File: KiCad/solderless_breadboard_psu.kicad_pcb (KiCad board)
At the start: 4 copper layers, 55 x 51 mm, 87 parts, among them IC301 MCP73831T-2ACI_OT, IC302 BQ29737DSER, IC401 TLV62569DBVR, IC501 FT232RL-REEL, J201 Barrel_Jack_Switch_Pin3Ring, J301 BM02B-GHS-TBT_LF__SN__N_, J501 Conn_01x09_Pin, J502 Conn_01x09_Pin, J503 Conn_01x06_Pin, J504 USB_C_Receptacle_USB2.0_16P, J601 Conn_02x03_Odd_Even, J602 Conn_02x03_Odd_Even, Q301 DMG3415U-7, Q302 T2N7002AK, Q303 T2N7002AK, U401 TPS61040DBVR, U501 USBLC6-2SC6

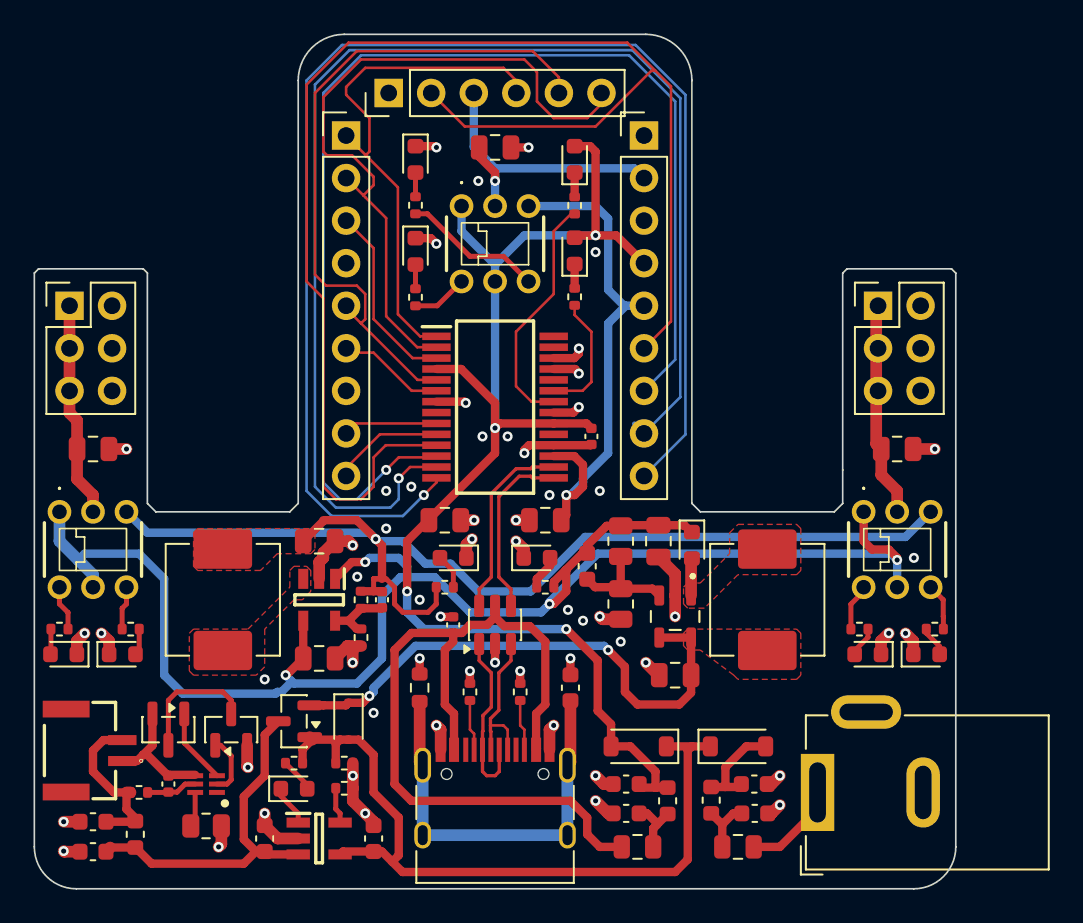
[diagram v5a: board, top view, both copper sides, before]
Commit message: PCB DRC fixes
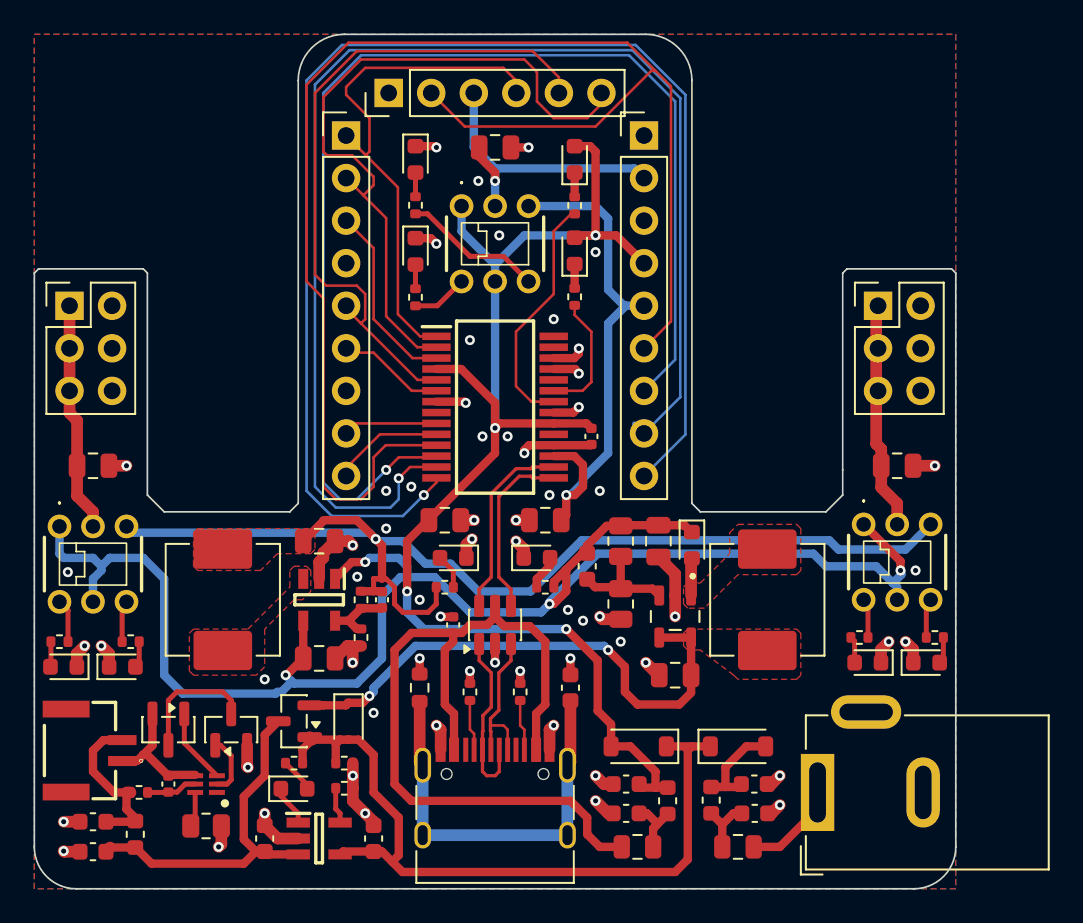
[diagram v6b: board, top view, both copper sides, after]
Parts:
- moved C601 1.00 mm to (26.0, 72.2)
- moved C602 1.00 mm to (74.0, 72.2)
- moved S601 0.87 mm to (24.0, 75.9)
- moved D601 0.75 mm to (24.2, 84.2)
- moved D602 0.75 mm to (27.8, 84.2)
- moved R601 0.75 mm to (24.0, 82.8)
- moved R602 0.75 mm to (28.2, 82.8)
- moved S602 0.75 mm to (72.0, 75.8)
- moved D603 0.50 mm to (72.2, 84.0)
- moved D604 0.50 mm to (75.8, 84.0)
- moved R603 0.50 mm to (71.8, 82.5), turned to 0 degrees
- moved R604 0.50 mm to (76.2, 82.5), turned to 180 degrees
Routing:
- net VCC_L: track 12.9 -> 13.8 mm
- net VCC_R: track 12.9 -> 13.6 mm
- net GND: vias 59 -> 63
- added copper zone on B.Cu, net GND
- added copper zone on F.Cu, net GND
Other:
- outline, holes or cut-outs redrawn

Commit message: Fill BOM table
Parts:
- C401, C402, C404, C406, C501, C503, C601, C602, C603: footprint Capacitor_SMD:C_0805_2012Metric -> Capacitor_SMD:C_0603_1608Metric
- R305, R402, R404: footprint Resistor_SMD:R_0805_2012Metric -> Resistor_SMD:R_0402_1005Metric
- R505: footprint Resistor_SMD:R_0603_1608Metric -> Resistor_SMD:R_0402_1005Metric
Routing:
- net GND: track 65.1 -> 65.8 mm, vias 63 -> 148
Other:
- board text added: "3V3"
- board text added: "5V"
- board text added: "CTS"
- board text added: "DCD"
- board text added: "DSR"
- board text added: "DTR"
- board text added: "FT232RL REEL"
- board text added: "GND"
- board text added: "PWREN"
- board text added: "RI"
- board text added: "RTS"
- board text added: "RX"
- board text added: "RXD"
- board text added: "SLP"
- board text added: "TEN"
- board text added: "TX"
- board text added: "TXD"
- board text added: "VCC"

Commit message: Production files
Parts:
- D401: footprint Diode_SMD:D_0603_1608Metric -> Diode_SMD:D_SMA
- R505: value DNP, 1MR -> 1MR
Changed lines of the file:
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@@
 			)
 		)
-		(property "Value" "DNP, 1MR"
+		(property "Value" "1MR"
 			(at 0 1.17 90)
 			(layer "F.Fab")
@@
 			(at 0 -1.17 0)
 			(layer "F.SilkS")
+			(hide yes)
 			(effects
 				(font
@@
 			(at 0 1.17 0)
 			(layer "F.Fab")
+			(hide yes)
 			(effects
 				(font
@@
 		)
 	)
-	(footprint "Diode_SMD:D_0603_1608Metric"
+	(footprint "Diode_SMD:D_SMA"
 		(layer "F.Cu")
 		(at 61.75 77 -90)
-		(descr "Diode SMD 0603 (1608 Metric), square (rectangular) end terminal, IPC-7351 nominal, (Body size source: http://www.tortai-tech.com/upload/download/2011102023233369053.pdf), generated with kicad-footprint-generator")
-		(tags "diode")
+		(descr "Diode SMA (DO-214AC)")
+		(tags "Diode SMA (DO-214AC)")
 		(property "Reference" "D401"
-			(at 0 -1.43 90)
+			(at 0 -2.5 270)
 			(layer "F.SilkS")
-			(hide yes)
 			(effects
 				(font
@@
 		)
 		(property "Value" "SS14"
-			(at 0 1.43 90)
+			(at 0 2.6 270)
 			(layer "F.Fab")
-			(hide yes)
 			(effects
 				(font
@@
 			)
 		)
-		(property "Datasheet" "https://www.vishay.com/docs/88746/ss12.pdf"
-			(at 0 0 90)
-			(layer "F.Fab")
-			(hide yes)
-			(effects
-				(font
-					(size 1.27 1.27)
-					(thickness 0.15)
-				)
-			)
-		)
-		(property "Description" "40V 1A Schottky Diode, SMA"
-			(at 0 0 90)
+		(property "Datasheet" "https://www.lcsc.com/datasheet/C266551.pdf"
+			(at 0 0 270)
+			(unlocked yes)
 			(layer "F.Fab")
 			(hide yes)
@@
 			)
 		)
-		(property "Manufacturer" "Schottky Diode"
+		(property "Description" "Diode 40V 1A Surface Mount SMA(DO-214AC)"
 			(at 0 0 270)
 			(unlocked yes)
@@
 			(effects
 				(font
-					(size 1 1)
+					(size 1.27 1.27)
 					(thickness 0.15)
 				)
 			)
 		)
-		(property "Manufacturer Product Number" "SD0603S040S0R2"
+		(property "Manufacturer" "BORN"
 			(at 0 0 270)
 			(unlocked yes)
@@
 			)
 		)
-		(property "Manufacturer Part Number" "JSMSEMI"
+		(property "Manufacturer Part Number" "SS14"
 			(at 0 0 270)
 			(unlocked yes)
@@
 		(attr smd)
 		(fp_line
-			(start -1.485 0.735)
-			(end 0.8 0.735)
+			(start -3.51 1.65)
+			(end 2 1.65)
 			(stroke
 				(width 0.12)
@@
 		)
 		(fp_line
-			(start -1.485 -0.735)
-			(end -1.485 0.735)
+			(start -3.51 -1.65)
+			(end -3.51 1.65)
 			(stroke
 				(width 0.12)
@@
 		)
 		(fp_line
-			(start 0.8 -0.735)
-			(end -1.485 -0.735)
+			(start -3.51 -1.65)
+			(end 2 -1.65)
 			(stroke
 				(width 0.12)
@@
 			(layer "F.SilkS")
 		)
-		(fp_rect
-			(start -1.48 -0.73)
-			(end 1.48 0.73)
+		(fp_line
+			(start -3.5 1.75)
+			(end -3.5 -1.75)
 			(stroke
 				(width 0.05)
 				(type solid)
 			)
-			(fill no)
 			(layer "F.CrtYd")
 		)
 		(fp_line
-			(start -0.8 0.4)
-			(end 0.8 0.4)
+			(start 3.5 1.75)
+			(end -3.5 1.75)
+			(stroke
+				(width 0.05)
+				(type solid)
+			)
+			(layer "F.CrtYd")
+		)
+		(fp_line
+			(start -3.5 -1.75)
+			(end 3.5 -1.75)
+			(stroke
+				(width 0.05)
+				(type solid)
+			)
+			(layer "F.CrtYd")
+		)
+		(fp_line
+			(start 3.5 -1.75)
+			(end 3.5 1.75)
+			(stroke
+				(width 0.05)
+				(type solid)
+			)
+			(layer "F.CrtYd")
+		)
+		(fp_line
+			(start -2.3 1.5)
+			(end -2.3 -1.5)
 			(stroke
 				(width 0.1)
@@
 		)
 		(fp_line
-			(start 0.8 0.4)
-			(end 0.8 -0.4)
+			(start 2.3 1.5)
+			(end -2.3 1.5)
 			(stroke
 				(width 0.1)
@@
 		)
 		(fp_line
-			(start -0.8 -0.1)
-			(end -0.8 0.4)
+			(start 0.50118 0.75032)
+			(end 0.50118 -0.79908)
 			(stroke
 				(width 0.1)
@@
 		)
 		(fp_line
-			(start -0.5 -0.4)
-			(end -0.8 -0.1)
+			(start -0.64944 0.00102)
+			(end 0.50118 0.75032)
 			(stroke
 				(width 0.1)
@@
 		)
 		(fp_line
-			(start 0.8 -0.4)
-			(end -0.5 -0.4)
+			(start -0.64944 0.00102)
+			(end -1.55114 0.00102)
+			(stroke
+				(width 0.1)
+				(type solid)
+			)
+			(layer "F.Fab")
+		)
+		(fp_line
+			(start -0.64944 0.00102)
+			(end 0.50118 -0.79908)
+			(stroke
+				(width 0.1)
+				(type solid)
+			)
+			(layer "F.Fab")
+		)
+		(fp_line
+			(start 0.50118 0.00102)
+			(end 1.4994 0.00102)
+			(stroke
+				(width 0.1)
+				(type solid)
+			)
+			(layer "F.Fab")
+		)
+		(fp_line
+			(start -0.64944 -0.79908)
+			(end -0.64944 0.80112)
+			(stroke
+				(width 0.1)
+				(type solid)
+			)
+			(layer "F.Fab")
+		)
+		(fp_line
+			(start 2.3 -1.5)
+			(end 2.3 1.5)
+			(stroke
+				(width 0.1)
+				(type solid)
+			)
+			(layer "F.Fab")
+		)
+		(fp_line
+			(start 2.3 -1.5)
+			(end -2.3 -1.5)
 			(stroke
 				(width 0.1)
@@
 		)
 		(fp_text user "${REFERENCE}"
-			(at 0 0 90)
+			(at 0 -2.5 270)
 			(layer "F.Fab")
 			(effects
 				(font
-					(size 0.4 0.4)
-					(thickness 0.06)
+					(size 1 1)
+					(thickness 0.15)
 				)
 			)
 		)
 		(pad "1" smd roundrect
-			(at -0.7875 0 270)
-			(size 0.875 0.95)
+			(at -2 0 270)
+			(size 2.5 1.8)
 			(layers "F.Cu" "F.Mask" "F.Paste")
-			(roundrect_rratio 0.25)
+			(roundrect_rratio 0.1388888889)
 			(net 11 "+5V")
 			(pinfunction "K")
@@
 		)
 		(pad "2" smd roundrect
-			(at 0.7875 0 270)
-			(size 0.875 0.95)
+			(at 2 0 270)
+			(size 2.5 1.8)
 			(layers "F.Cu" "F.Mask" "F.Paste")
-			(roundrect_rratio 0.25)
+			(roundrect_rratio 0.1388888889)
 			(net 21 "/[4]Buck Boost converter/BST_SW_5V")
 			(pinfunction "A")
@@
 		)
 		(embedded_fonts no)
-		(model "${KICAD9_3DMODEL_DIR}/Diode_SMD.3dshapes/D_0603_1608Metric.step"
+		(model "${KICAD9_3DMODEL_DIR}/Diode_SMD.3dshapes/D_SMA.step"
 			(offset
 				(xyz 0 0 0)
